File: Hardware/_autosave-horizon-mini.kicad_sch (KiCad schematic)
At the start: 77 parts, among them J2 Conn_01x02_Pin, J3 Micro_SD_Card_Det1, J7 USB_C_Receptacle_USB2.0_16P, J8 Conn_02x03_Counter_Clockwise, Q1 BSS138, Q10 DMG2301L, U1 TPS82130, U16 AP2112K-3.3, U2 TPS61092, U3 LTC4412xS6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

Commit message: please liam fix decop caps
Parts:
- C11, C7, C8, C9: value 0.1uF -> 100nF
- C12: value 10uF -> 100nF
- C6: value F1uF -> 100nF
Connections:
- net +3.3V: now also C11.2, C12.2, C7.2, C8.2, C9.2, U5.17 (VDDIO), U5.36 (VDDIO), U5.44 (VDDIN), U5.6 (VDDANA)
- net GND: now also C11.1, C12.1, C6.1, C7.1, C8.1, C9.1; no longer C6.2
- net at U5.43 (VDDCORE): now also C6.2; no longer C6.1

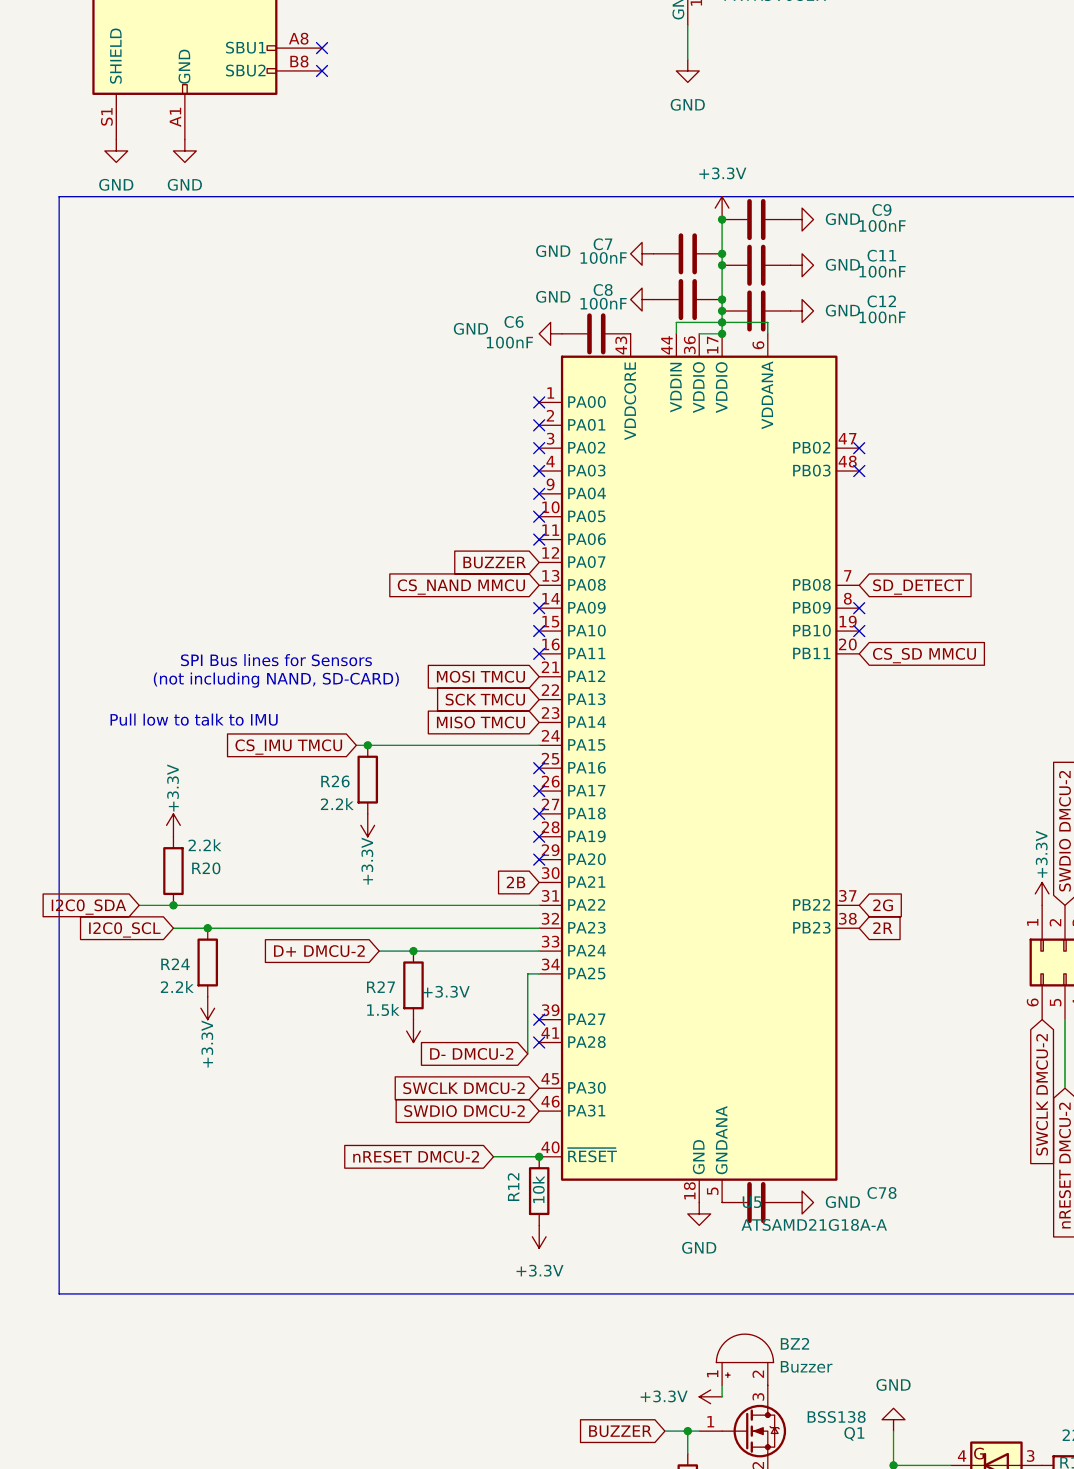
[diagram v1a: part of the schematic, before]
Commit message: fixed decop caps schematic and routes (plz check my work scooter)
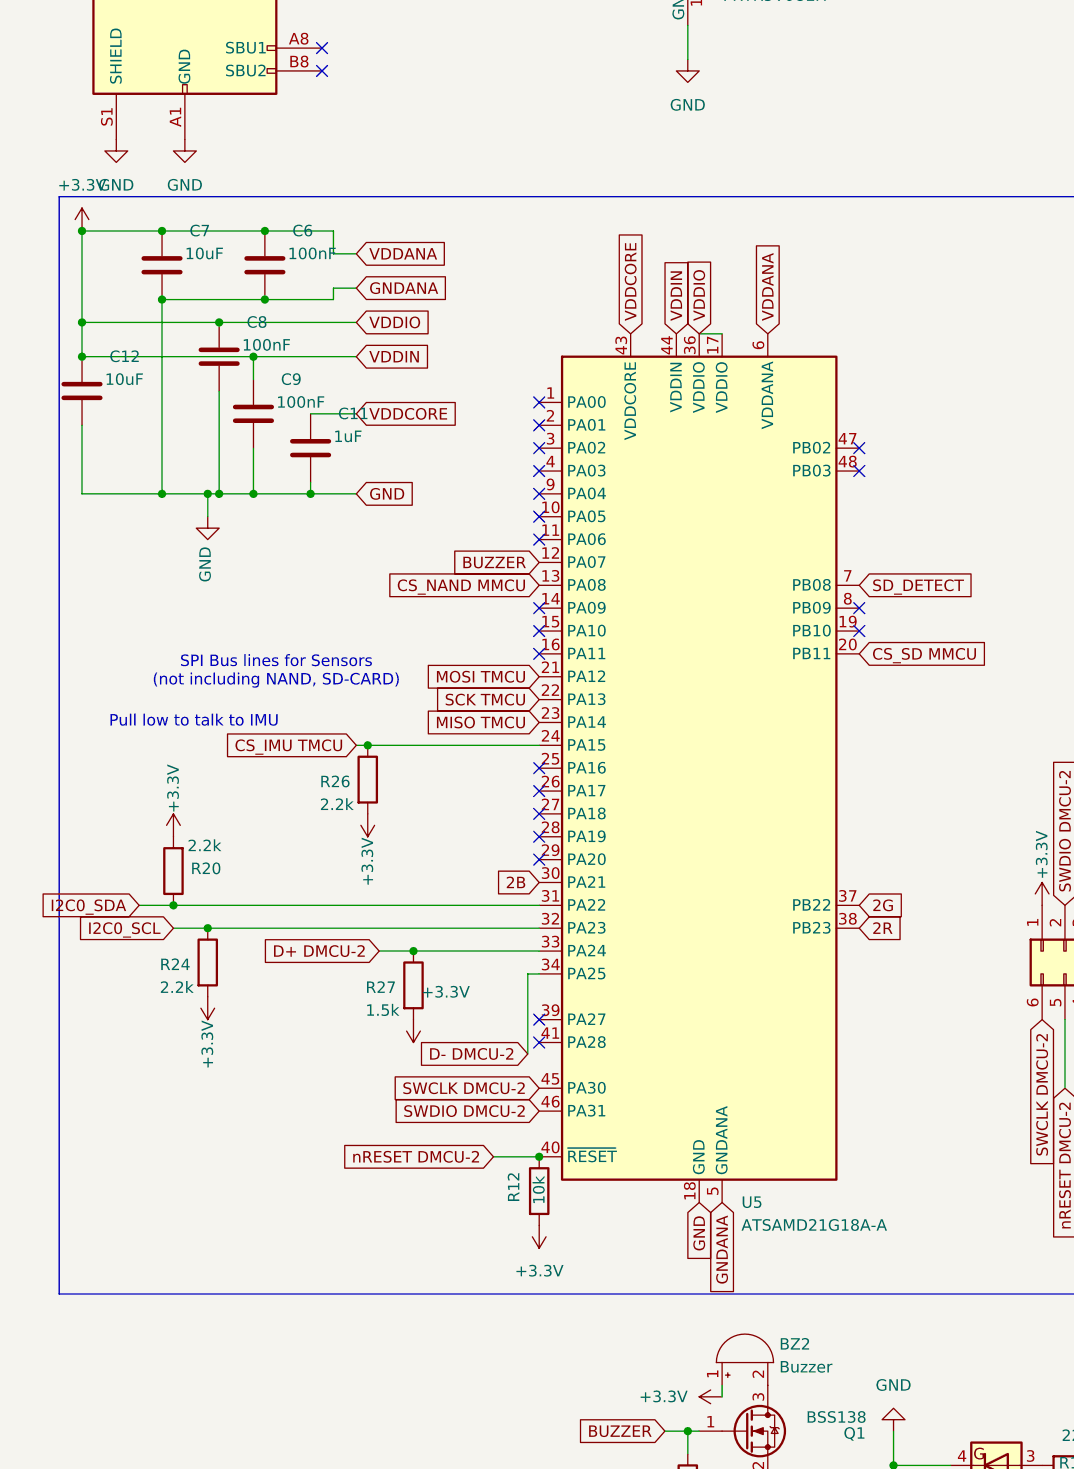
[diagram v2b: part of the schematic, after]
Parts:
- removed C78: 100nF, Capacitor_SMD:C_0603_1608Metric, symbol Device:C
- C11: value 100nF -> 1uF
- C12, C7: value 100nF -> 10uF
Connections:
- net +3.3V: now also C12.1, C6.1, C7.1, C8.1, C9.1; no longer C11.2, C12.2, C7.2, C8.2, C9.2
- net GND: now also C11.2, C12.2, C6.2, C7.2, C8.2, C9.2, U5.5 (GNDANA); no longer C11.1, C12.1, C6.1, C7.1, C8.1, C9.1
- net VDDCORE: now reaches U5.43 (VDDCORE)
- net VDDCORE: now also C11.1; no longer C6.2
